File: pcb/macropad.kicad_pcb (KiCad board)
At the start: 2 copper layers, 88 x 66.5 mm, 19 parts, among them J1 OLED_DISPLAY, SW1 SW_Push, SW2 SW_Push, SW3 SW_Push, SW4 SW_Push, SW5 RotaryEncoder_Switch, SW6 SW_Push, U1 Seeed Studio XIAO RP2040

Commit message: V1.2 - Fixed the LED symbols and retraced everything
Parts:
- D7, D8, D9: footprint Hackpad:SK6812MINI-E_fixed -> LED_SMD:LED_SK6812MINI-E_3.2x2.8mm_P1.5mm_ReverseMount
- moved D7 0.50 mm to (172.5, 106.5), turned to 0 degrees
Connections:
- D7 pad 1: VCC -> GND
- D7 pad 2: unconnected-(D7-DOUT-Pad2) -> Net-(D7-DIN)
- D7 pad 3: GND -> VCC
- D7 pad 4: Net-(D7-DIN) -> unconnected-(D7-DOUT-Pad4)
- D8 pad 1: VCC -> GND
- D8 pad 2: Net-(D7-DIN) -> Net-(D8-DOUT)
- D8 pad 3: GND -> VCC
- D8 pad 4: Net-(D8-DIN) -> Net-(D7-DIN)
- D9 pad 1: VCC -> GND
- D9 pad 2: Net-(D8-DIN) -> Net-(D9-DOUT)
- D9 pad 3: GND -> VCC
- D9 pad 4: Net-(D9-DIN) -> Net-(D8-DOUT)
- U1 pad 11: Net-(D9-DIN) -> Net-(D9-DOUT)
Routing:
- net Net-(D8-DIN): track 75.9 -> 0.00 mm
- net VCC: track 262.2 -> 336.7 mm, vias 0 -> 1
- net Net-(D8-DOUT): track 0.00 -> 72.6 mm
- net GND: track 216.7 -> 266.9 mm, vias 0 -> 1
- net Net-(D9-DOUT): track 0.00 -> 22.9 mm
- net Net-(D9-DIN): track 15.6 -> 0.00 mm
- net Net-(D7-DIN): track 127.1 -> 114.2 mm
- net Net-(D3-A): track 34.8 -> 33.6 mm, vias 0 -> 1

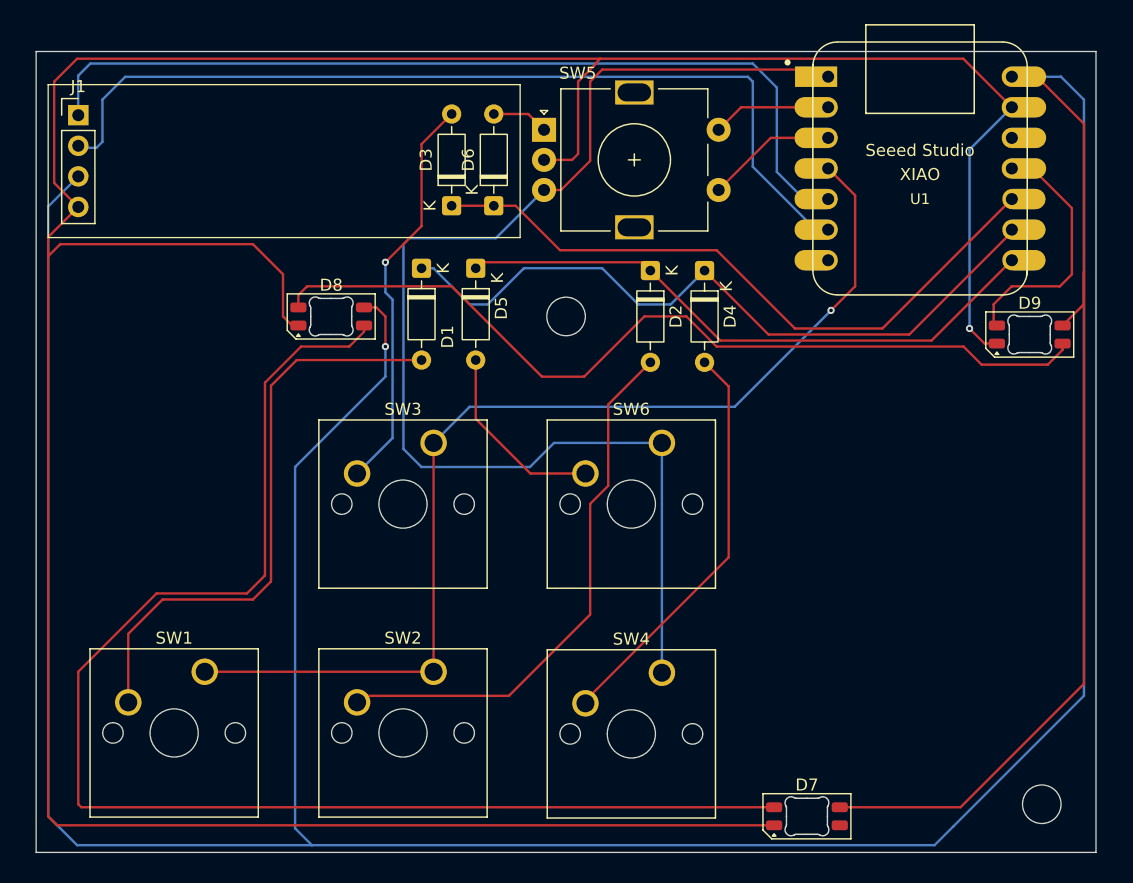
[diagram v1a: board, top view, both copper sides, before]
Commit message: V1.3 - Added switch LEDs and GND fields
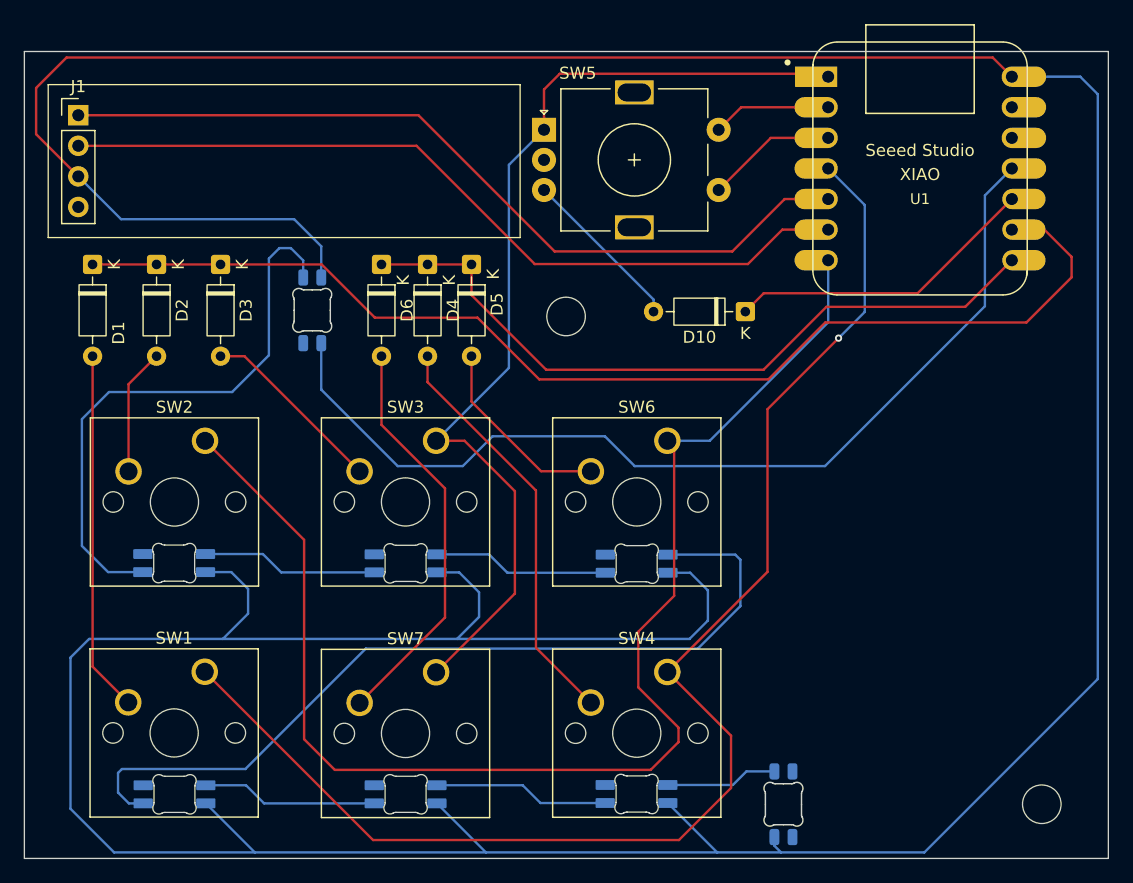
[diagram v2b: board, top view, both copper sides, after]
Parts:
- added D10: D, Diode_THT:D_DO-35_SOD27_P7.62mm_Horizontal, F.Cu at (167.4, 64.6)
- added D11: SK6812MINI-E, Cherry-MX:MX_SK6812MINI-E, F.Cu at (139.2, 80.4)
- added D12: SK6812MINI-E, Cherry-MX:MX_SK6812MINI-E, F.Cu at (158.4, 80.4)
- added D13: SK6812MINI-E, Cherry-MX:MX_SK6812MINI-E, F.Cu at (120.0, 99.6)
- added D14: SK6812MINI-E, Cherry-MX:MX_SK6812MINI-E, F.Cu at (139.2, 99.6)
- added D15: SK6812MINI-E, Cherry-MX:MX_SK6812MINI-E, F.Cu at (158.3, 99.6)
- added SW7: SW_Push, Button_Switch_Keyboard:SW_Cherry_MX_1.00u_PCB, F.Cu at (141.7, 94.5)
- D7, D8: moved to B.Cu
- D9: footprint LED_SMD:LED_SK6812MINI-E_3.2x2.8mm_P1.5mm_ReverseMount -> Cherry-MX:MX_SK6812MINI-E
- moved D9 72.4 mm to (120.0, 80.4)
- moved D2 41.0 mm to (118.5, 60.7)
- moved D1 27.3 mm to (113.2, 60.7)
- moved SW2 27.0 mm to (122.5, 75.3)
- moved D4 23.0 mm to (141.0, 60.7)
- moved D3 19.8 mm to (123.8, 60.7), turned to -90 degrees
- moved D6 10.5 mm to (137.2, 60.7), turned to -90 degrees
- moved D7 2.19 mm to (170.6, 105.5), turned to -90 degrees
- moved D8 1.66 mm to (131.4, 64.5), turned to 90 degrees
- moved SW6 0.48 mm to (160.9, 75.3)
- moved D5 0.47 mm to (144.7, 60.7)
- moved SW4 0.45 mm to (160.9, 94.5)
- moved SW3 0.28 mm to (141.7, 75.3)
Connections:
- D2 pad 1: Row 2 -> Row 1
- D3 pad 1: Row 3 -> Row 1
- D4 pad 1: Row 1 -> Row 2
- D6 pad 1: Row 3 -> Row 2
- D7 pad 2: Net-(D7-DIN) -> Net-(D15-DOUT)
- D8 pad 2: Net-(D8-DOUT) -> LED-IN
- D8 pad 4: Net-(D7-DIN) -> Net-(D8-DOUT)
- D9 pad 2: Net-(D9-DOUT) -> Net-(D8-DOUT)
- D9 pad 4: Net-(D8-DOUT) -> Net-(D11-DIN)
- SW2 pad 1: Column 1 -> Column 2
- SW3 pad 1: Column 1 -> Column 3
- SW4 pad 1: Column 2 -> Column 1
- SW5 pad A: Net-(D6-A) -> Column 3
- SW5 pad B: Column 2 -> Net-(D10-A)
- U1 pad 1: Column 2 -> Column 3
- U1 pad 11: Net-(D9-DOUT) -> LED-IN
- U1 pad 7: unconnected-(U1-PB08_A6_D6_TX-Pad7) -> Column 2
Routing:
- net GND: track 266.9 -> 0.00 mm, vias 1 -> 0
- net Net-(D7-DIN): track 114.2 -> 0.00 mm
- net Column 3: track 0.00 -> 83.1 mm
- net LED-IN: track 0.00 -> 81.5 mm
- net Net-(D12-DOUT): track 0.00 -> 71.5 mm
- net VCC: track 336.7 -> 375.7 mm, vias 1 -> 0
- net Row 1: track 59.8 -> 96.3 mm
- net Net-(D2-A): track 45.4 -> 10.5 mm
- net Net-(D6-A): track 4.71 -> 33.9 mm
- net Row 3: track 55.2 -> 26.0 mm
- net Net-(D8-DOUT): track 72.6 -> 47.3 mm
- net Column 1: track 89.1 -> 113.0 mm
- net Net-(D9-DOUT): track 22.9 -> 0.00 mm
- net Net-(D1-A): track 49.0 -> 30.0 mm
- net Net-(D3-A): track 33.6 -> 15.5 mm, vias 1 -> 0
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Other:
- board size 88 x 66.5 mm -> 90 x 67 mm
